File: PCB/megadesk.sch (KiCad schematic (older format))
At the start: 23 parts, among them CON1 ISP, J1 Interface, J2 FFC, U1 L7812, U2 L7805, U3 ATTINY841-SSU, U4 MCP2003B

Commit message: Schematic mostly updated for KiCad v5. PCB layout untouched.
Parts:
- BZ1: symbol Buzzer -> device:Buzzer
- C1, C4, C6: symbol C -> device:C
- C2, C3, C5: symbol CP -> device:CP
- CON1: symbol AVR-ISP-6 -> Connector:AVR-ISP-6
- D1, D2: symbol D -> device:D
- J1: symbol Conn_01x03 -> Connector_Generic:Conn_01x03
- J2: symbol Conn_01x10 -> Connector_Generic:Conn_01x10
- R1, R3, R4, R5, R6: symbol R -> device:R
- TP1, TP2: symbol TEST -> Connector:TestPoint
- U1: symbol L7812 -> Regulator_Linear:L7812; Details (none) -> STMicroelectronics L78M12CDT
- U2: symbol L7805 -> Regulator_Linear:L7805
- U3: symbol ATTINY841-SSU -> MCU_Microchip_ATtiny:ATtiny841-SSU
- U4: symbol MCP2003B -> custom:MCP2003B
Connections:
- no-connect marks 1 -> 0
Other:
- moved on the sheet: C4, TP1, TP2, U3

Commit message: Switch to ceramic caps
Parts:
- BZ1: footprint !Custom:Buzzer_PUI_SMT-1141-T-5-R -> Buzzer_Beeper:Buzzer_CUI_CPT-9019S-SMT
- C2: value 10uf -> 10uf-DNP; footprint Capacitors_SMD:CP_Elec_5x5.3 -> Capacitor_SMD:C_1206_3216Metric_Pad1.42x1.75mm_HandSolder; symbol device:CP -> device:C
- C3, C5: footprint Capacitors_SMD:CP_Elec_4x4.5 -> Capacitor_SMD:C_1206_3216Metric_Pad1.42x1.75mm_HandSolder; symbol device:CP -> device:C
- C4, C6: footprint Capacitors_SMD:C_1206_HandSoldering -> Capacitor_SMD:C_1206_3216Metric_Pad1.42x1.75mm_HandSolder
- J2: footprint !Custom:FFC_10 -> Connector_FFC-FPC:TE_1-84953-0_1x10-1MP_P1.0mm_Horizontal
- R1, R3, R4, R5, R6: footprint Resistors_SMD:R_1206_HandSoldering -> Resistor_SMD:R_1206_3216Metric
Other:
- moved on the sheet: BZ1, C1, C4, C6, CON1, D1, D2, J1, J2, R1, R3, R4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

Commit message: V2 ready to go
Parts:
- C1: footprint Capacitors_SMD:C_1206_HandSoldering -> Capacitor_SMD:C_1206_3216Metric
- C2, C3, C4, C5, C6: footprint Capacitor_SMD:C_1206_3216Metric_Pad1.42x1.75mm_HandSolder -> Capacitor_SMD:C_1206_3216Metric
- J2: footprint Connector_FFC-FPC:TE_1-84953-0_1x10-1MP_P1.0mm_Horizontal -> !Custom:FFC_10
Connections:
- no-connect marks 0 -> 11
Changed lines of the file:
@@
 F 0 "C5" H 3125 1650 50  0000 L CNN
 F 1 "0.1uf" H 3125 1450 50  0000 L CNN
-F 2 "Capacitor_SMD:C_1206_3216Metric_Pad1.42x1.75mm_HandSolder" H 3138 1400 50  0001 C CNN
+F 2 "Capacitor_SMD:C_1206_3216Metric" H 3138 1400 50  0001 C CNN
 F 3 "" H 3100 1550 50  0001 C CNN
 	1    3100 1550
@@
 F 0 "C3" H 1825 1650 50  0000 L CNN
 F 1 "0.1uf" H 1825 1450 50  0000 L CNN
-F 2 "Capacitor_SMD:C_1206_3216Metric_Pad1.42x1.75mm_HandSolder" H 1838 1400 50  0001 C CNN
+F 2 "Capacitor_SMD:C_1206_3216Metric" H 1838 1400 50  0001 C CNN
 F 3 "" H 1800 1550 50  0001 C CNN
 	1    1800 1550
@@
 F 0 "C6" H 8425 3300 50  0000 L CNN
 F 1 "220pF" H 8425 3100 50  0000 L CNN
-F 2 "Capacitor_SMD:C_1206_3216Metric_Pad1.42x1.75mm_HandSolder" H 8438 3050 50  0001 C CNN
+F 2 "Capacitor_SMD:C_1206_3216Metric" H 8438 3050 50  0001 C CNN
 F 3 "" H 8400 3200 50  0001 C CNN
 	1    8400 3200
@@
 F 0 "C1" H 850 1550 50  0000 L CNN
 F 1 "0.33uF" H 750 1450 50  0000 L CNN
-F 2 "Capacitors_SMD:C_1206_HandSoldering" H 788 1400 50  0001 C CNN
+F 2 "Capacitor_SMD:C_1206_3216Metric" H 788 1400 50  0001 C CNN
 F 3 "" H 750 1550 50  0001 C CNN
 	1    750  1550
@@
 F 0 "C4" H 3675 2550 50  0000 L CNN
 F 1 "0.1uF" H 3400 2350 50  0000 L CNN
-F 2 "Capacitor_SMD:C_1206_3216Metric_Pad1.42x1.75mm_HandSolder" H 3688 2300 50  0001 C CNN
+F 2 "Capacitor_SMD:C_1206_3216Metric" H 3688 2300 50  0001 C CNN
 F 3 "" H 3650 2450 50  0001 C CNN
 	1    3650 2450
@@
 F 0 "C2" H 1575 1650 50  0000 L CNN
 F 1 "10uf-DNP" H 1350 1350 50  0000 L CNN
-F 2 "Capacitor_SMD:C_1206_3216Metric_Pad1.42x1.75mm_HandSolder" H 1588 1400 50  0001 C CNN
+F 2 "Capacitor_SMD:C_1206_3216Metric" H 1588 1400 50  0001 C CNN
 F 3 "" H 1550 1550 50  0001 C CNN
 	1    1550 1550
@@
 F 0 "J2" H 6350 2000 50  0000 C CNN
 F 1 "FFC" H 6350 900 50  0000 C CNN
-F 2 "Connector_FFC-FPC:TE_1-84953-0_1x10-1MP_P1.0mm_Horizontal" H 6350 1500 50  0001 C CNN
+F 2 "!Custom:FFC_10" H 6350 1500 50  0001 C CNN
 F 3 "" H 6350 1500 50  0001 C CNN
 	1    6350 1500
@@
 Wire Wire Line
 	750  1000 1750 1000
+NoConn ~ 5150 3800
+NoConn ~ 5150 3000
+NoConn ~ 5150 2700
+NoConn ~ 7600 2750
+NoConn ~ 6150 1100
+NoConn ~ 6150 1200
+NoConn ~ 6150 1300
+NoConn ~ 6150 1400
+NoConn ~ 6150 1800
+NoConn ~ 6150 1900
+NoConn ~ 6150 2000
 $EndSCHEMATC

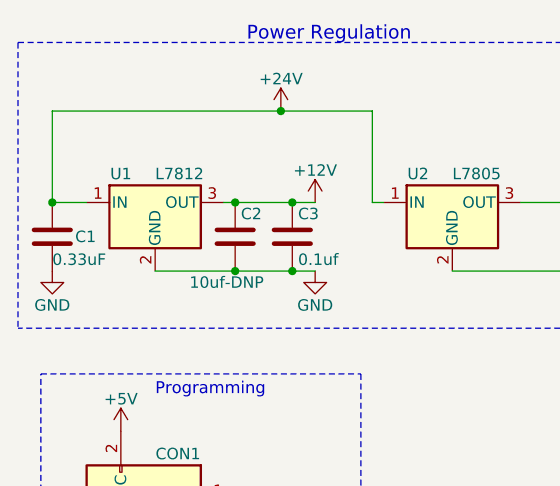
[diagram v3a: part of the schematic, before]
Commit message: Updated BOM with part numbers
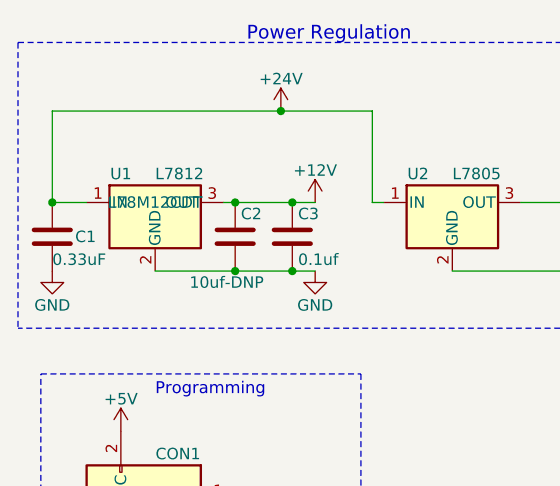
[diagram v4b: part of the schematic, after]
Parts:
- BZ1: Part Number (none) -> CPT-9019S-SM
- J2: Part Number (none) -> 1-84981-0
- U1: Part Number (none) -> L78M12CDT
- U2: Part Number (none) -> L78M05CDT
- U3: Part Number (none) -> ATTINY841-SSU
- U4: Part Number (none) -> MCP2003B-E/SN
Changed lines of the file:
@@
 F 2 "TO_SOT_Packages_SMD:TO-252-3_TabPin2" H 2525 1250 50  0001 L CIN
 F 3 "" H 2500 1350 50  0001 C CNN
+F 4 "L78M05CDT" H 2500 1400 50  0001 C CNN "Part Number"
 	1    2500 1400
 	1    0    0    -1
@@
 F 2 "Housings_SOIC:SOIC-8_3.9x4.9mm_Pitch1.27mm" H 7300 2950 50  0001 C CNN
 F 3 "" H 7300 2950 50  0001 C CNN
+F 4 "MCP2003B-E/SN" H 7200 2950 50  0001 C CNN "Part Number"
 	1    7200 2950
 	1    0    0    -1
@@
 F 2 "TO_SOT_Packages_SMD:TO-252-3_TabPin2" H 1225 1250 50  0001 L CIN
 F 3 "" H 1200 1350 50  0001 C CNN
-F 4 "STMicroelectronics L78M12CDT" H 1200 1400 60  0001 C CNN "Details"
+F 4 "L78M12CDT" H 1200 1400 50  0000 C CNN "Part Number"
+F 5 "STMicroelectronics L78M12CDT" H 1200 1400 60  0001 C CNN "Details"
 	1    1200 1400
 	1    0    0    -1
@@
 F 2 "Housings_SOIC:SOIC-14_3.9x8.7mm_Pitch1.27mm" H 4550 3100 50  0001 C CIN
 F 3 "" H 4550 3300 50  0001 C CNN
+F 4 "ATTINY841-SSU" H 4550 3300 50  0001 C CNN "Part Number"
 	1    4550 3300
 	1    0    0    -1
@@
 F 2 "!Custom:FFC_10" H 6350 1500 50  0001 C CNN
 F 3 "" H 6350 1500 50  0001 C CNN
+F 4 "1-84981-0" H 6350 1500 50  0001 C CNN "Part Number"
 	1    6350 1500
 	1    0    0    -1
@@
 F 2 "Buzzer_Beeper:Buzzer_CUI_CPT-9019S-SMT" V 5925 3600 50  0001 C CNN
 F 3 "" V 5925 3600 50  0001 C CNN
+F 4 "CPT-9019S-SM" H 5950 3500 50  0001 C CNN "Part Number"
 	1    5950 3500
 	1    0    0    -1

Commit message: Minor cleanup
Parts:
- U4: symbol custom:MCP2003B -> !Custom:MCP2003B
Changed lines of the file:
@@
 Programming
 $Comp
-L custom:MCP2003B U4
+L !Custom:MCP2003B U4
 U 1 1 5A826DCE
 P 7200 2950

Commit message: Updated a few things and clean up some backup files.
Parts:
- removed C2: 10uf-DNP, Capacitor_SMD:C_1206_3216Metric, symbol device:C
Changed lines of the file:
@@
 EESchema Schematic File Version 4
-LIBS:megadesk-cache
 EELAYER 26 0
 EELAYER END
@@
 $EndComp
 $Comp
-L device:C C2
-U 1 1 5AA206F9
-P 1550 1550
-F 0 "C2" H 1575 1650 50  0000 L CNN
-F 1 "10uf-DNP" H 1350 1350 50  0000 L CNN
-F 2 "Capacitor_SMD:C_1206_3216Metric" H 1588 1400 50  0001 C CNN
-F 3 "" H 1550 1550 50  0001 C CNN
-	1    1550 1550
-	1    0    0    -1
-$EndComp
-$Comp
 L Connector_Generic:Conn_01x10 J2
 U 1 1 5AA53CE2
@@
 	4300 1850 4300 950
 Wire Wire Line
-	1500 1400 1550 1400
-Wire Wire Line
 	7800 2250 7800 2350
 Wire Wire Line
@@
 Wire Wire Line
 	2500 1700 3100 1700
-Wire Wire Line
-	1200 1700 1550 1700
-Connection ~ 1550 1700
-Connection ~ 1550 1400
 Wire Wire Line
 	900  1400 750  1400
@@
 Wire Wire Line
 	6400 2650 6650 2650
-Wire Wire Line
-	1550 1700 1800 1700
-Wire Wire Line
-	1550 1400 1800 1400
 Wire Wire Line
 	4550 2400 4550 2300
@@
 NoConn ~ 6150 1900
 NoConn ~ 6150 2000
+Wire Wire Line
+	1500 1400 1800 1400
+Wire Wire Line
+	1200 1700 1800 1700
 $EndSCHEMATC
